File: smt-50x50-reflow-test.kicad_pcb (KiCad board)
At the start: 4 copper layers, 50 x 50 mm, 97 parts, among them J1 Conn_01x04_Pin, J2 Conn_01x02, J4 USB_C_Receptacle_USB2.0_14P, J8 Conn_01x04_Pin, J9 Conn_01x03_Pin, SW1 SW_Push, SW2 SW_Push, U1 ESP32-C6, U14 TMP117AIDRV, U15 BMP581, U16 TMP117AIDRV, U2 W25Q128JVS, U3 AP2112K-3.3, U4 LM317_TO-252, U5 LMR36520FADDA, U7 USBLC6-2SC6, Y1 48M

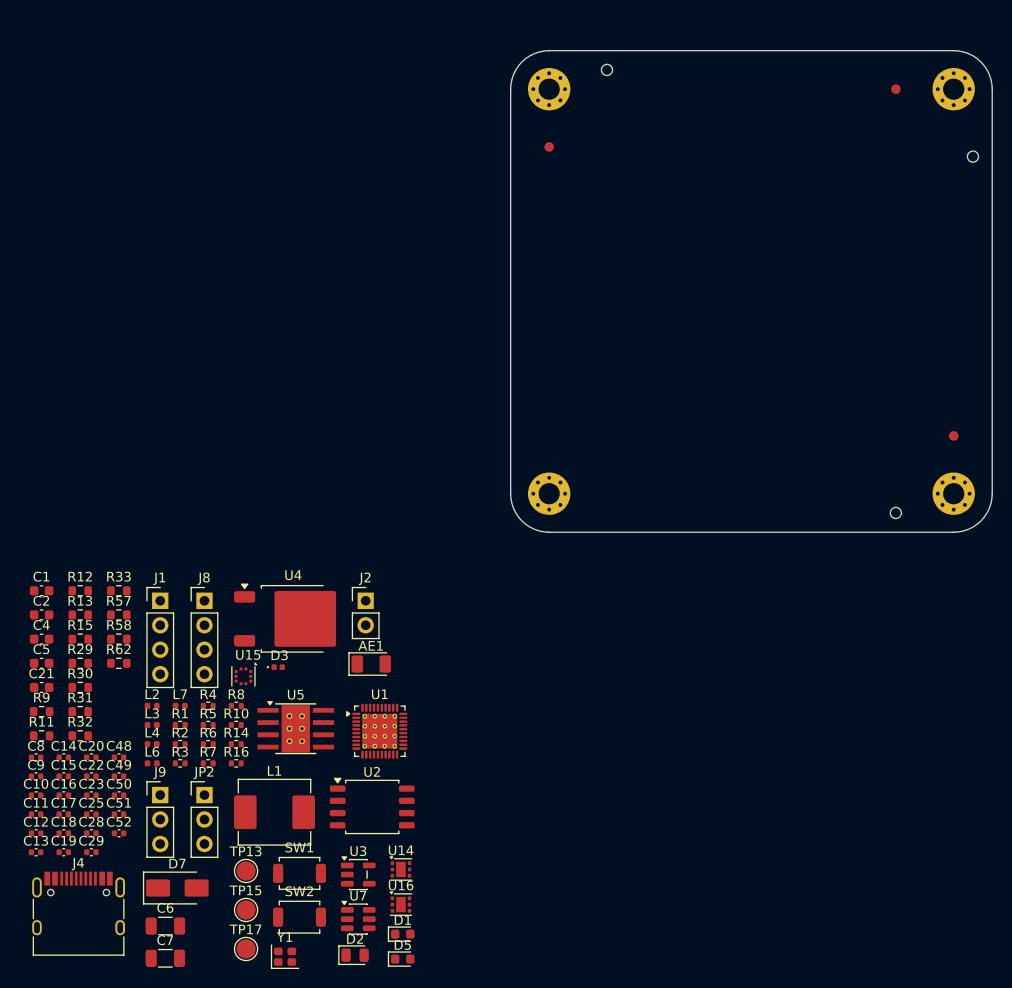
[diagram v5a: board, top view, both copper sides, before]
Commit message: pcb: initial rough placement
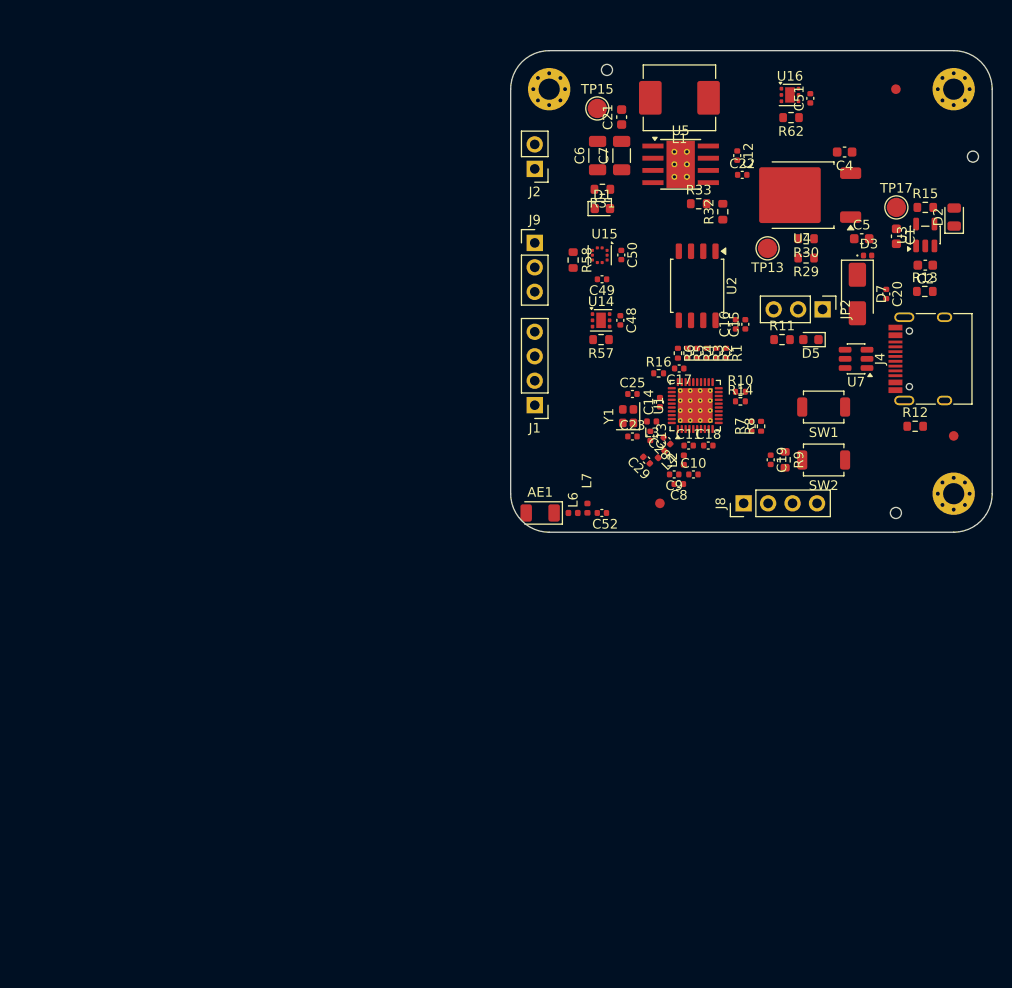
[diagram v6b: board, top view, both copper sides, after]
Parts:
- removed the REF** at (139.0, 121.0)
- moved J4 106.1 mm to (179.0, 107.0), turned to 90 degrees
- moved C51 103.3 mm to (166.1, 80.0), turned to 90 degrees
- moved TP17 102.4 mm to (175.1, 91.3)
- moved C12 101.2 mm to (158.5, 85.9), turned to -90 degrees
- moved D2 98.7 mm to (181.1, 92.3), turned to 90 degrees
- moved C2 98.7 mm to (178.1, 97.3), turned to 180 degrees
- moved R15 98.5 mm to (178.1, 91.3)
- moved C4 97.5 mm to (169.7, 85.5), turned to 180 degrees
- moved C1 96.1 mm to (175.1, 94.3), turned to -90 degrees
- moved C5 95.9 mm to (171.4, 94.5)
- moved C7 95.9 mm to (146.5, 85.9), turned to 90 degrees
- moved C20 95.5 mm to (174.0, 100.3), turned to -90 degrees
- moved R13 93.9 mm to (178.0, 100.0)
- moved D7 93.7 mm to (171.0, 100.3), turned to -90 degrees
- moved U16 93.3 mm to (164.0, 79.6)
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
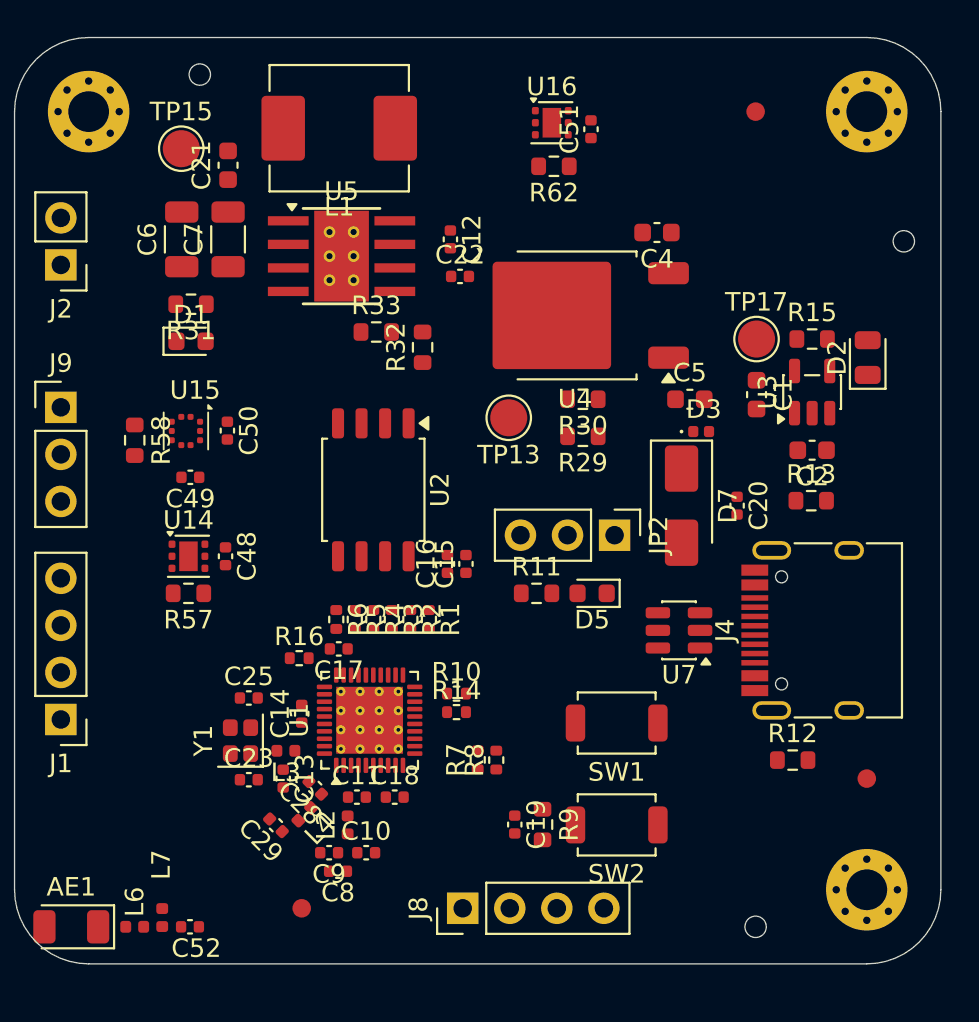
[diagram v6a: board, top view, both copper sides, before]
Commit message: pcb: placement refinement
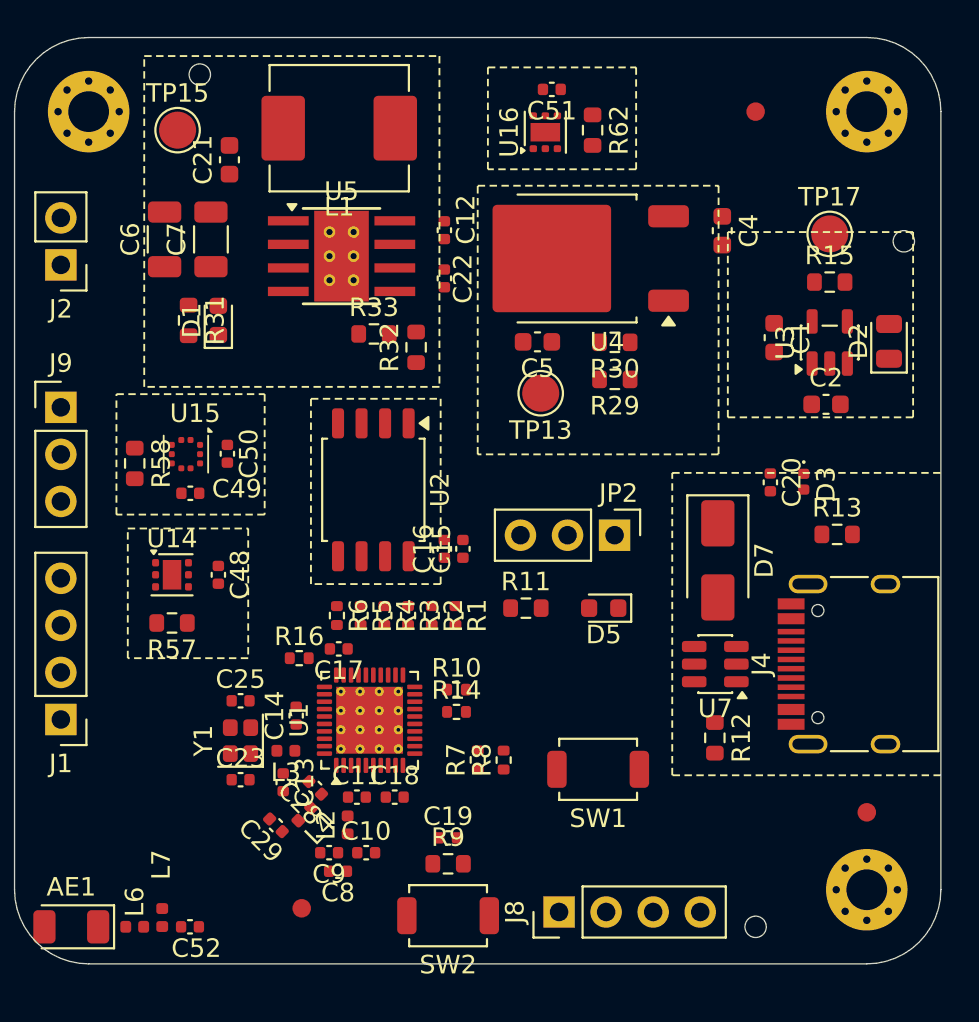
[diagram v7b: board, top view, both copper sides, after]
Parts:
- moved SW2 10.3 mm to (158.4, 122.4)
- moved C5 8.79 mm to (163.2, 91.4), turned to 180 degrees
- moved TP17 6.91 mm to (179.0, 85.6)
- moved D3 6.19 mm to (177.6, 98.9), turned to -90 degrees
- moved R9 5.52 mm to (158.4, 119.6), turned to 0 degrees
- moved J8 5.20 mm to (164.4, 122.2)
- moved R12 4.37 mm to (172.8, 112.8), turned to -90 degrees
- moved C19 3.67 mm to (158.4, 118.2), turned to 0 degrees
- moved D7 3.54 mm to (173.0, 103.2)
- moved C4 3.53 mm to (173.2, 85.4), turned to -90 degrees
- moved R29 3.52 mm to (167.4, 93.5)
- moved R30 3.52 mm to (167.4, 91.5)
- moved C1 3.22 mm to (176.0, 91.2)
- moved R15 3.22 mm to (179.0, 88.2)
- moved U4 3.07 mm to (165.3, 86.9)
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
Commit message: pcb: refine rf layout
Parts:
- moved AE1 0.70 mm to (138.6, 122.5)
- moved C52 0.70 mm to (145.0, 122.5)
- moved L7 0.70 mm to (143.5, 122.0)
- moved L6 0.70 mm to (142.0, 122.5)
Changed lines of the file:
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@@
 	(footprint "RF_Antenna:Johanson_2450AT18x100"
 		(layer "F.Cu")
-		(at 138.0625 123 180)
+		(at 138.55 122.5 180)
 		(descr "Johanson 2450AT43F0100 SMD antenna 2400-2500Mhz, -0.5dBi, https://www.johansontechnology.com/datasheets/2450AT18A100/2450AT18A100.pdf")
 		(tags "antenna")
@@
 			)
 			(layer "F.SilkS")
-			(net 112)
 		)
 		(fp_line
@@
 			)
 			(layer "F.SilkS")
-			(net 112)
 		)
 		(fp_line
@@
 			)
 			(layer "F.SilkS")
-			(net 112)
 		)
 		(fp_line
@@
 			)
 			(layer "F.CrtYd")
-			(net 112)
 		)
 		(fp_line
@@
 			)
 			(layer "F.CrtYd")
-			(net 112)
 		)
 		(fp_line
@@
 			)
 			(layer "F.CrtYd")
-			(net 112)
 		)
 		(fp_line
@@
 			)
 			(layer "F.CrtYd")
-			(net 112)
 		)
 		(fp_line
@@
 			)
 			(layer "F.Fab")
-			(net 112)
 		)
 		(fp_line
@@
 			)
 			(layer "F.Fab")
-			(net 112)
 		)
 		(fp_line
@@
 			)
 			(layer "F.Fab")
-			(net 112)
 		)
 		(fp_line
@@
 			)
 			(layer "F.Fab")
-			(net 112)
 		)
 		(fp_line
@@
 			)
 			(layer "F.Fab")
-			(net 112)
 		)
 		(fp_text user "${REFERENCE}"
@@
 	(footprint "Capacitor_SMD:C_0402_1005Metric"
 		(layer "F.Cu")
-		(at 144.47 123 180)
+		(at 144.9575 122.5 180)
 		(descr "Capacitor SMD 0402 (1005 Metric), square (rectangular) end terminal, IPC-7351 nominal, (Body size source: IPC-SM-782 page 76, https://www.pcb-3d.com/wordpress/wp-content/uploads/ipc-sm-782a_amendment_1_and_2.pdf), generated with kicad-footprint-generator")
 		(tags "capacitor")
@@
 			)
 			(layer "F.SilkS")
-			(net 112)
 		)
 		(fp_line
@@
 			)
 			(layer "F.SilkS")
-			(net 112)
 		)
 		(fp_line
@@
 			)
 			(layer "F.CrtYd")
-			(net 112)
 		)
 		(fp_line
@@
 			)
 			(layer "F.CrtYd")
-			(net 112)
 		)
 		(fp_line
@@
 			)
 			(layer "F.CrtYd")
-			(net 112)
 		)
 		(fp_line
@@
 			)
 			(layer "F.CrtYd")
-			(net 112)
 		)
 		(fp_line
@@
 			)
 			(layer "F.Fab")
-			(net 112)
 		)
 		(fp_line
@@
 			)
 			(layer "F.Fab")
-			(net 112)
 		)
 		(fp_line
@@
 			)
 			(layer "F.Fab")
-			(net 112)
 		)
 		(fp_line
@@
 			)
 			(layer "F.Fab")
-			(net 112)
 		)
 		(fp_text user "${REFERENCE}"
@@
 	(footprint "Inductor_SMD:L_0402_1005Metric"
 		(layer "F.Cu")
-		(at 142.97 122.5 -90)
+		(at 143.4575 122 -90)
 		(descr "Inductor SMD 0402 (1005 Metric), square (rectangular) end terminal, IPC-7351 nominal, (Body size source: http://www.tortai-tech.com/upload/download/2011102023233369053.pdf), generated with kicad-footprint-generator")
 		(tags "inductor")
@@
 			)
 			(layer "F.CrtYd")
-			(net 112)
 		)
 		(fp_line
@@
 			)
 			(layer "F.CrtYd")
-			(net 112)
 		)
 		(fp_line
@@
 			)
 			(layer "F.CrtYd")
-			(net 112)
 		)
 		(fp_line
@@
 			)
 			(layer "F.CrtYd")
-			(net 112)
 		)
 		(fp_line
@@
 			)
 			(layer "F.Fab")
-			(net 112)
 		)
 		(fp_line
@@
 			)
 			(layer "F.Fab")
-			(net 112)
 		)
 		(fp_line
@@
 			)
 			(layer "F.Fab")
-			(net 112)
 		)
 		(fp_line
@@
 			)
 			(layer "F.Fab")
-			(net 112)
 		)
 		(fp_text user "${REFERENCE}"
@@
 	(footprint "Inductor_SMD:L_0402_1005Metric"
 		(layer "F.Cu")
-		(at 141.485 123)
+		(at 141.9725 122.5)
 		(descr "Inductor SMD 0402 (1005 Metric), square (rectangular) end terminal, IPC-7351 nominal, (Body size source: http://www.tortai-tech.com/upload/download/2011102023233369053.pdf), generated with kicad-footprint-generator")
 		(tags "inductor")
@@
 			)
 			(layer "F.CrtYd")
-			(net 112)
 		)
 		(fp_line
@@
 			)
 			(layer "F.CrtYd")
-			(net 112)
 		)
 		(fp_line
@@
 			)
 			(layer "F.CrtYd")
-			(net 112)
 		)
 		(fp_line
@@
 			)
 			(layer "F.CrtYd")
-			(net 112)
 		)
 		(fp_line
@@
 			)
 			(layer "F.Fab")
-			(net 112)
 		)
 		(fp_line
@@
 			)
 			(layer "F.Fab")
-			(net 112)
 		)
 		(fp_line
@@
 			)
 			(layer "F.Fab")
-			(net 112)
 		)
 		(fp_line
@@
 			)
 			(layer "F.Fab")
-			(net 112)
 		)
 		(fp_text user "${REFERENCE}"
@@
 		(tags "Through hole pin header THT 1x04 2.54mm single row")
 		(property "Reference" "J1"
-			(at 0 -2.38 0)
+			(at -2.7 -0.79 0)
 			(layer "F.SilkS")
 			(effects
@@
 	)
 	(gr_line
+		(start 135 114)
+		(end 143.5 114)
+		(stroke
+			(width 0.1)
+			(type dash)
+		)
+		(layer "F.SilkS")
+	)
+	(gr_line
 		(start 185 114.82)
 		(end 170.5 114.82)
@@
 		(layer "F.SilkS")
 	)
+	(gr_line
+		(start 147 120)
+		(end 143.5 120)
+		(stroke
+			(width 0.1)
+			(type dash)
+		)
+		(layer "F.SilkS")
+	)
 	(gr_rect
 		(start 173.5 85.5)
@@
 		(layer "F.SilkS")
 	)
+	(gr_line
+		(start 147 120)
+		(end 147 125)
+		(stroke
+			(width 0.1)
+			(type dash)
+		)
+		(layer "F.SilkS")
+	)
+	(gr_line
+		(start 143.5 114)
+		(end 143.5 120)
+		(stroke
+			(width 0.1)
+			(type dash)
+		)
+		(layer "F.SilkS")
+	)
 	(gr_arc
 		(start 181 75)
@@
 		(polygon
 			(pts
-				(xy 135.3125 125.25) (xy 135.3125 114.75) (xy 142.5625 114.75) (xy 142.5625 125.25)
+				(xy 135 125) (xy 135 114.1) (xy 142.95 114.1) (xy 142.95 125)
 			)
 		)
